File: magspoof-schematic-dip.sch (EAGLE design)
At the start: 8 parts, among them IC1 L293D, U1 ATTINY85-20SU

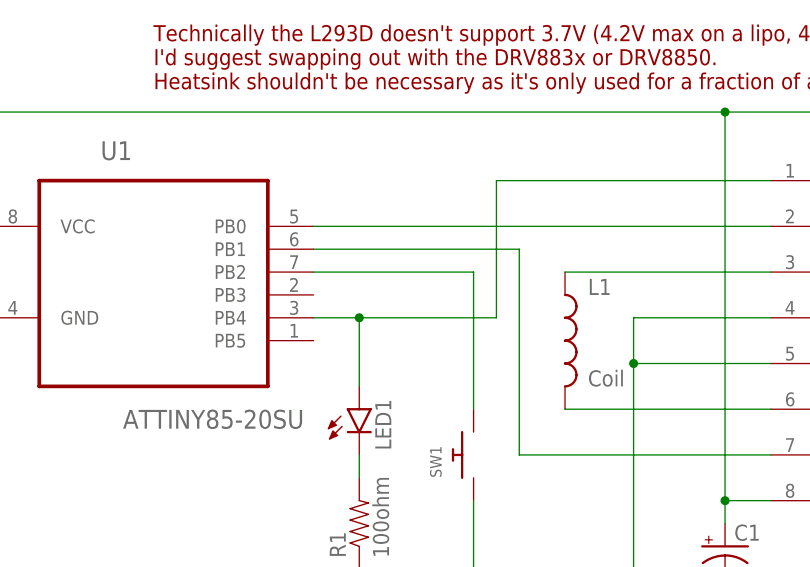
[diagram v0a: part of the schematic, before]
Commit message: Fixed wrong pin connection, PB4->PB3 (thanks @shellster)
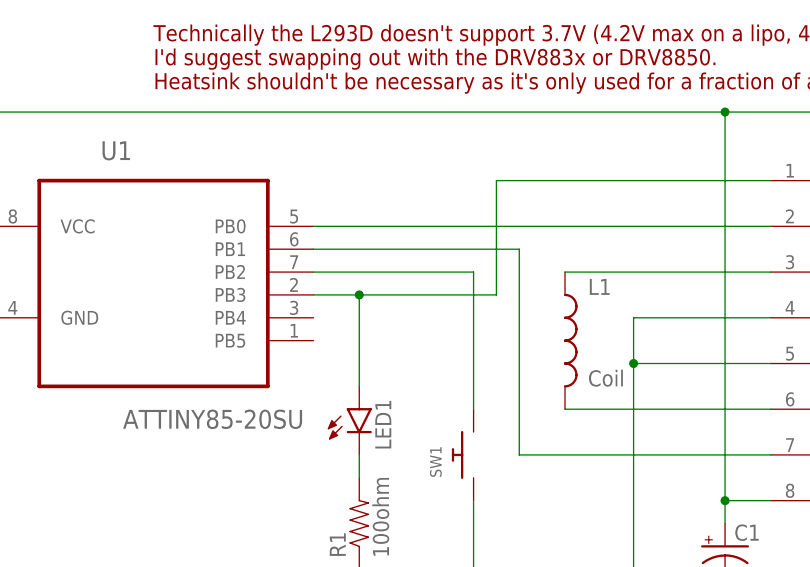
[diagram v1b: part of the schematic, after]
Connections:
- net N$5: now also U1.PB3; no longer U1.PB4
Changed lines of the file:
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@@
 <?xml version="1.0" encoding="utf-8"?>
 <!DOCTYPE eagle SYSTEM "eagle.dtd">
-<eagle version="7.5.0">
+<eagle version="7.5.1">
 <drawing>
 <settings>
@@
 <net name="N$5" class="0">
 <segment>
-<wire x1="127" y1="101.6" x2="127" y2="116.84" width="0.1524" layer="91"/>
+<wire x1="127" y1="104.14" x2="127" y2="116.84" width="0.1524" layer="91"/>
 <pinref part="IC1" gate="G$1" pin="1-2EN"/>
 <wire x1="127" y1="116.84" x2="157.48" y2="116.84" width="0.1524" layer="91"/>
-<pinref part="U1" gate="A" pin="PB4"/>
+<pinref part="U1" gate="A" pin="PB3"/>
+<wire x1="127" y1="104.14" x2="111.76" y2="104.14" width="0.1524" layer="91"/>
 <pinref part="LED1" gate="G$1" pin="A"/>
-<wire x1="106.68" y1="101.6" x2="111.76" y2="101.6" width="0.1524" layer="91"/>
-<wire x1="111.76" y1="101.6" x2="111.76" y2="93.98" width="0.1524" layer="91"/>
-<wire x1="127" y1="101.6" x2="111.76" y2="101.6" width="0.1524" layer="91"/>
-<junction x="111.76" y="101.6"/>
-</segment>
-</net>
+<wire x1="111.76" y1="104.14" x2="106.68" y2="104.14" width="0.1524" layer="91"/>
+<wire x1="111.76" y1="93.98" x2="111.76" y2="104.14" width="0.1524" layer="91"/>
+<junction x="111.76" y="104.14"/>
+</segment>
+</net>
